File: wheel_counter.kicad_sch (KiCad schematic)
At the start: 112 parts, among them J2 Conn_01x02_Pin, U2 IRLML6344TRPBF, U3 IRLML6344TRPBF

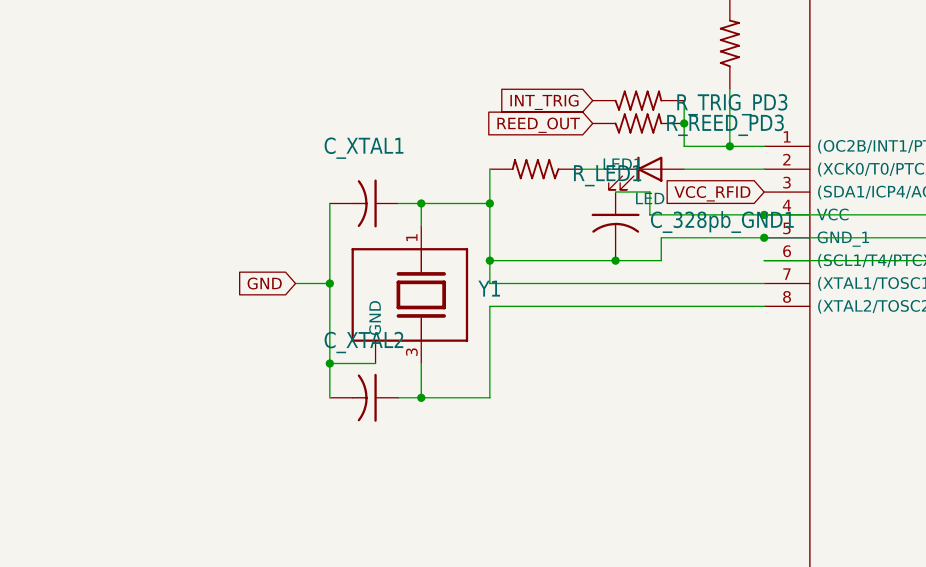
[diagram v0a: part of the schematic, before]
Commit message: fix ground
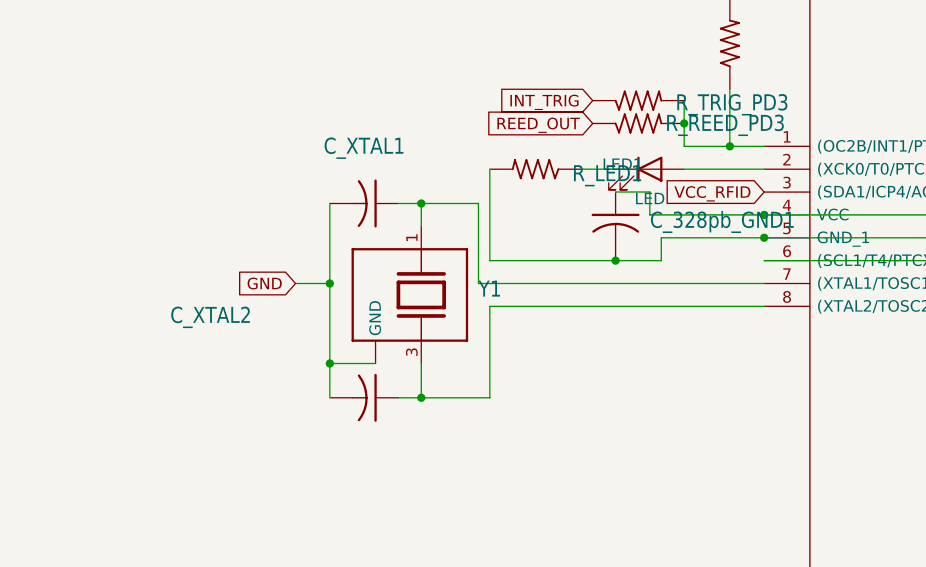
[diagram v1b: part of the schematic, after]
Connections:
- net GND: no longer 328pb1.7 ((XTAL1/TOSC1)_PB6), C_XTAL1.1, Y1.1
- new net: 328pb1.7 ((XTAL1/TOSC1)_PB6), C_XTAL1.1, Y1.1
